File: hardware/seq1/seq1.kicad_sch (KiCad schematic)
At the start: 0 parts

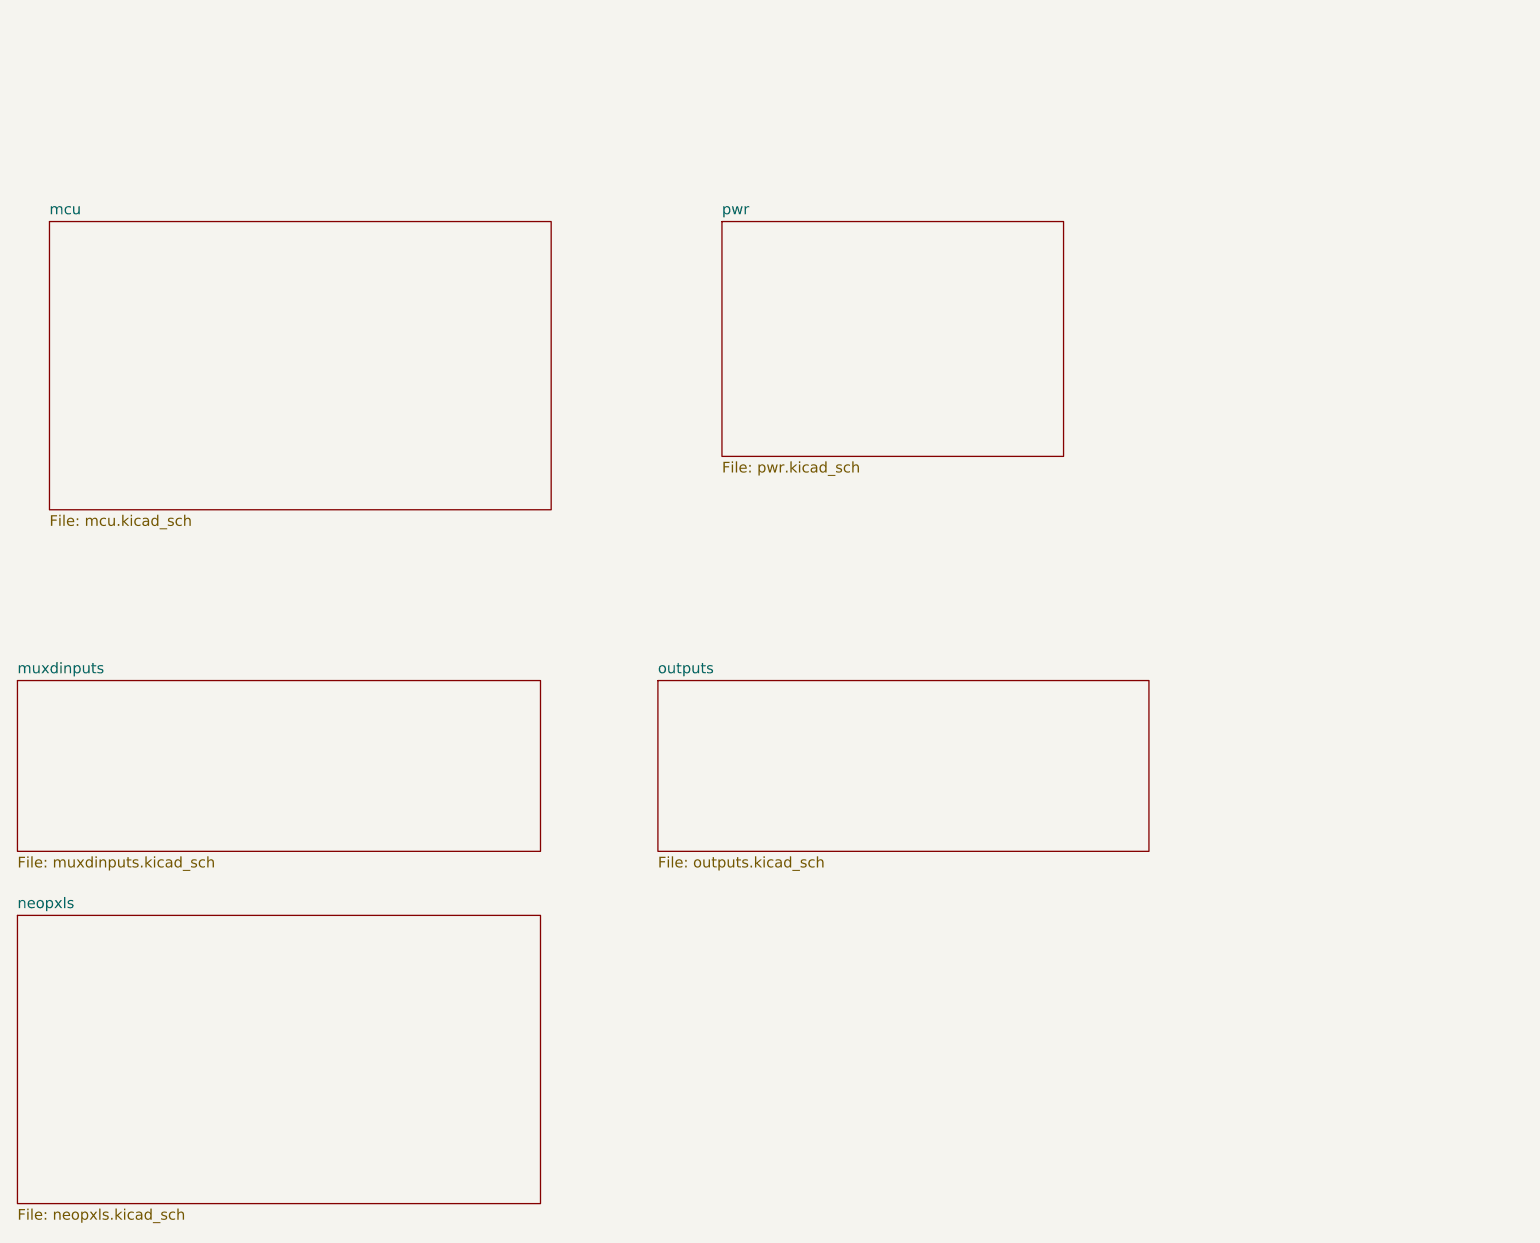
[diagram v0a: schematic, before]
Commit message: Some schematic cleanup
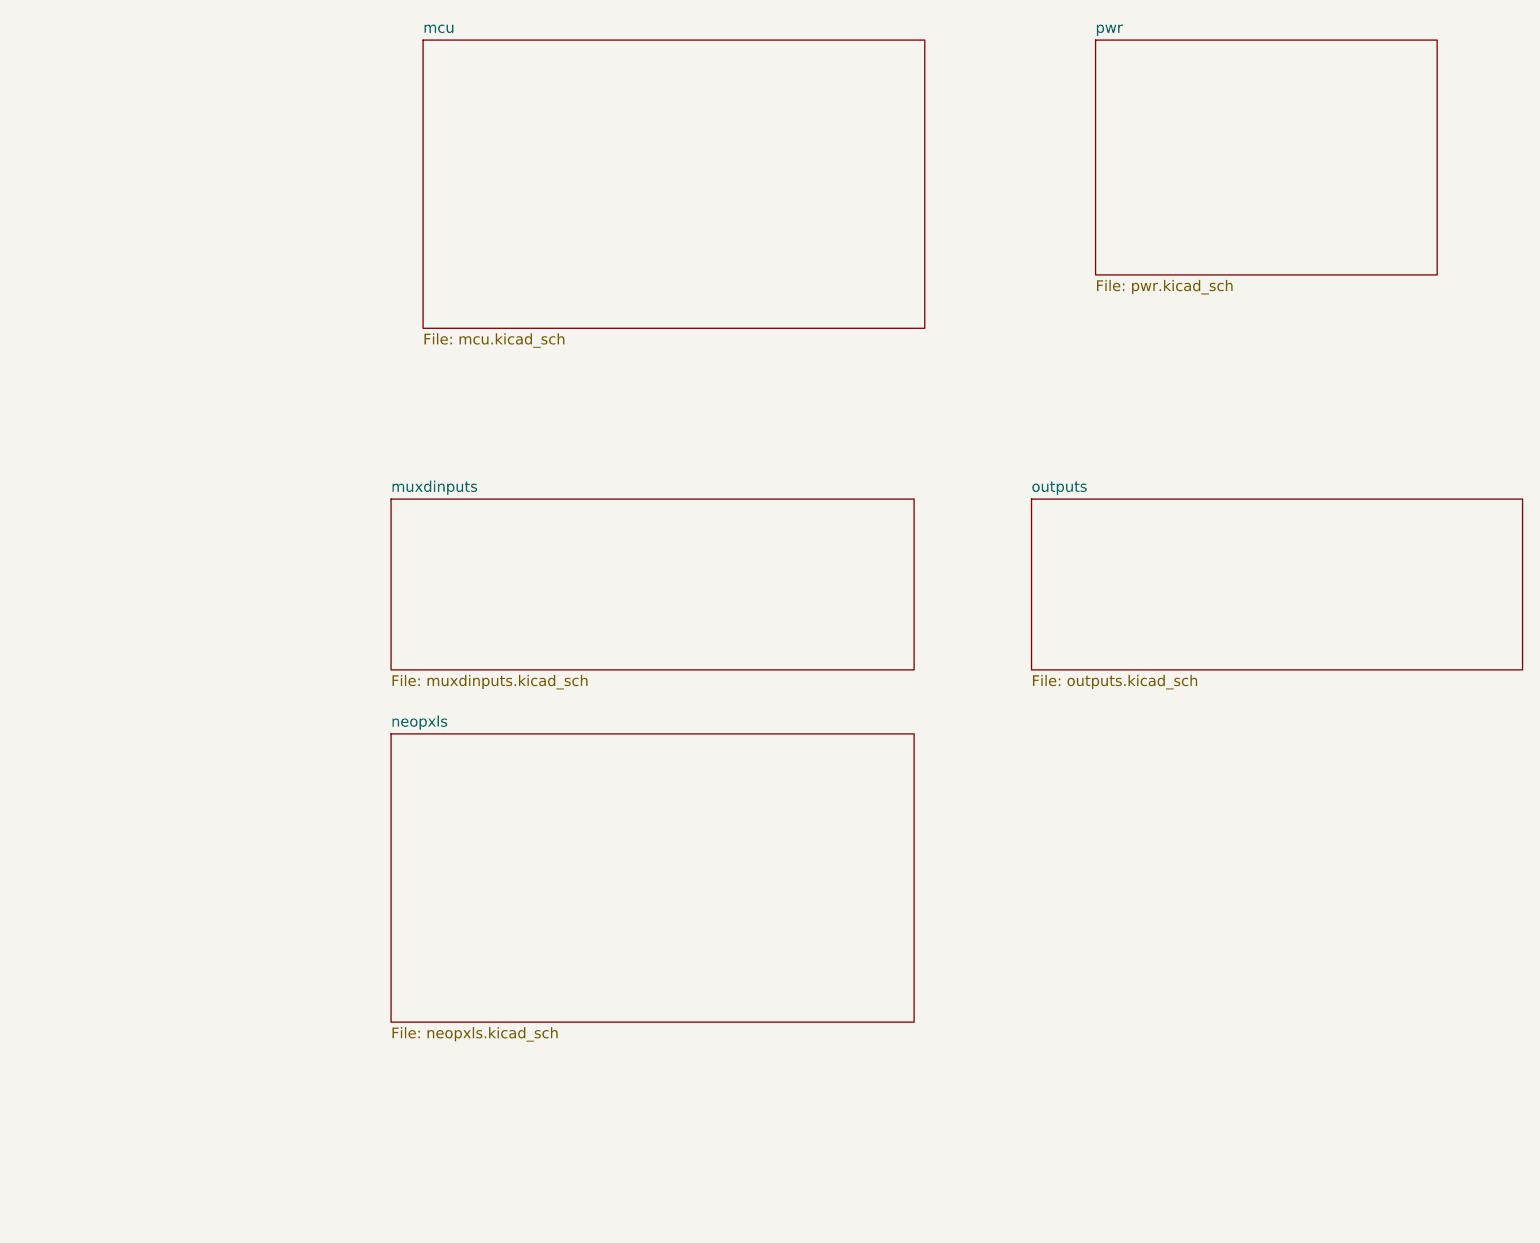
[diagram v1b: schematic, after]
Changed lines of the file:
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@@
 	(title_block
 		(title "Sequencer")
-		(date "2025-11-07")
+		(date "2025-12-28")
 		(rev "2.0")
 		(company "idyllm")
@@
 	)
 	(sheet
-		(at 21.59 125.73)
+		(at 66.04 104.14)
 		(size 62.23 20.32)
 		(exclude_from_sim no)
@@
 		)
 		(property "Sheetname" "muxdinputs"
-			(at 21.59 125.0184 0)
+			(at 66.04 103.4284 0)
 			(effects
 				(font
@@
 		)
 		(property "Sheetfile" "muxdinputs.kicad_sch"
-			(at 21.59 146.6346 0)
+			(at 66.04 125.0446 0)
 			(effects
 				(font
@@
 	)
 	(sheet
-		(at 21.59 153.67)
+		(at 66.04 132.08)
 		(size 62.23 34.29)
 		(exclude_from_sim no)
@@
 		)
 		(property "Sheetname" "neopxls"
-			(at 21.59 152.9584 0)
+			(at 66.04 131.3684 0)
 			(effects
 				(font
@@
 		)
 		(property "Sheetfile" "neopxls.kicad_sch"
-			(at 21.59 188.5446 0)
+			(at 66.04 166.9546 0)
 			(effects
 				(font
@@
 	)
 	(sheet
-		(at 97.79 125.73)
+		(at 142.24 104.14)
 		(size 58.42 20.32)
 		(exclude_from_sim no)
@@
 		)
 		(property "Sheetname" "outputs"
-			(at 97.79 125.0184 0)
+			(at 142.24 103.4284 0)
 			(effects
 				(font
@@
 		)
 		(property "Sheetfile" "outputs.kicad_sch"
-			(at 97.79 146.6346 0)
+			(at 142.24 125.0446 0)
 			(effects
 				(font
@@
 	)
 	(sheet
-		(at 105.41 71.12)
+		(at 149.86 49.53)
 		(size 40.64 27.94)
 		(exclude_from_sim no)
@@
 		)
 		(property "Sheetname" "pwr"
-			(at 105.41 70.4084 0)
+			(at 149.86 48.8184 0)
 			(effects
 				(font
@@
 		)
 		(property "Sheetfile" "pwr.kicad_sch"
-			(at 105.41 99.6446 0)
+			(at 149.86 78.0546 0)
 			(effects
 				(font
@@
 	)
 	(sheet
-		(at 25.4 71.12)
+		(at 69.85 49.53)
 		(size 59.69 34.29)
 		(exclude_from_sim no)
@@
 		)
 		(property "Sheetname" "mcu"
-			(at 25.4 70.4084 0)
+			(at 69.85 48.8184 0)
 			(effects
 				(font
@@
 		)
 		(property "Sheetfile" "mcu.kicad_sch"
-			(at 25.4 105.9946 0)
-			(effects
-				(font
+			(at 69.85 84.4046 0)
+			(effects
+				(font
